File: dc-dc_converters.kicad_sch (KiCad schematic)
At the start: 61 parts, among them J3 JST_SH_1x4_SM04B-SRSS-TB-LF-SN, J4 Molex_Nano-Fit_1x2_105313-220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, U2 SIC477ED-T1-GE3, U3 AP62301WU-7, U4 AP62301WU-7

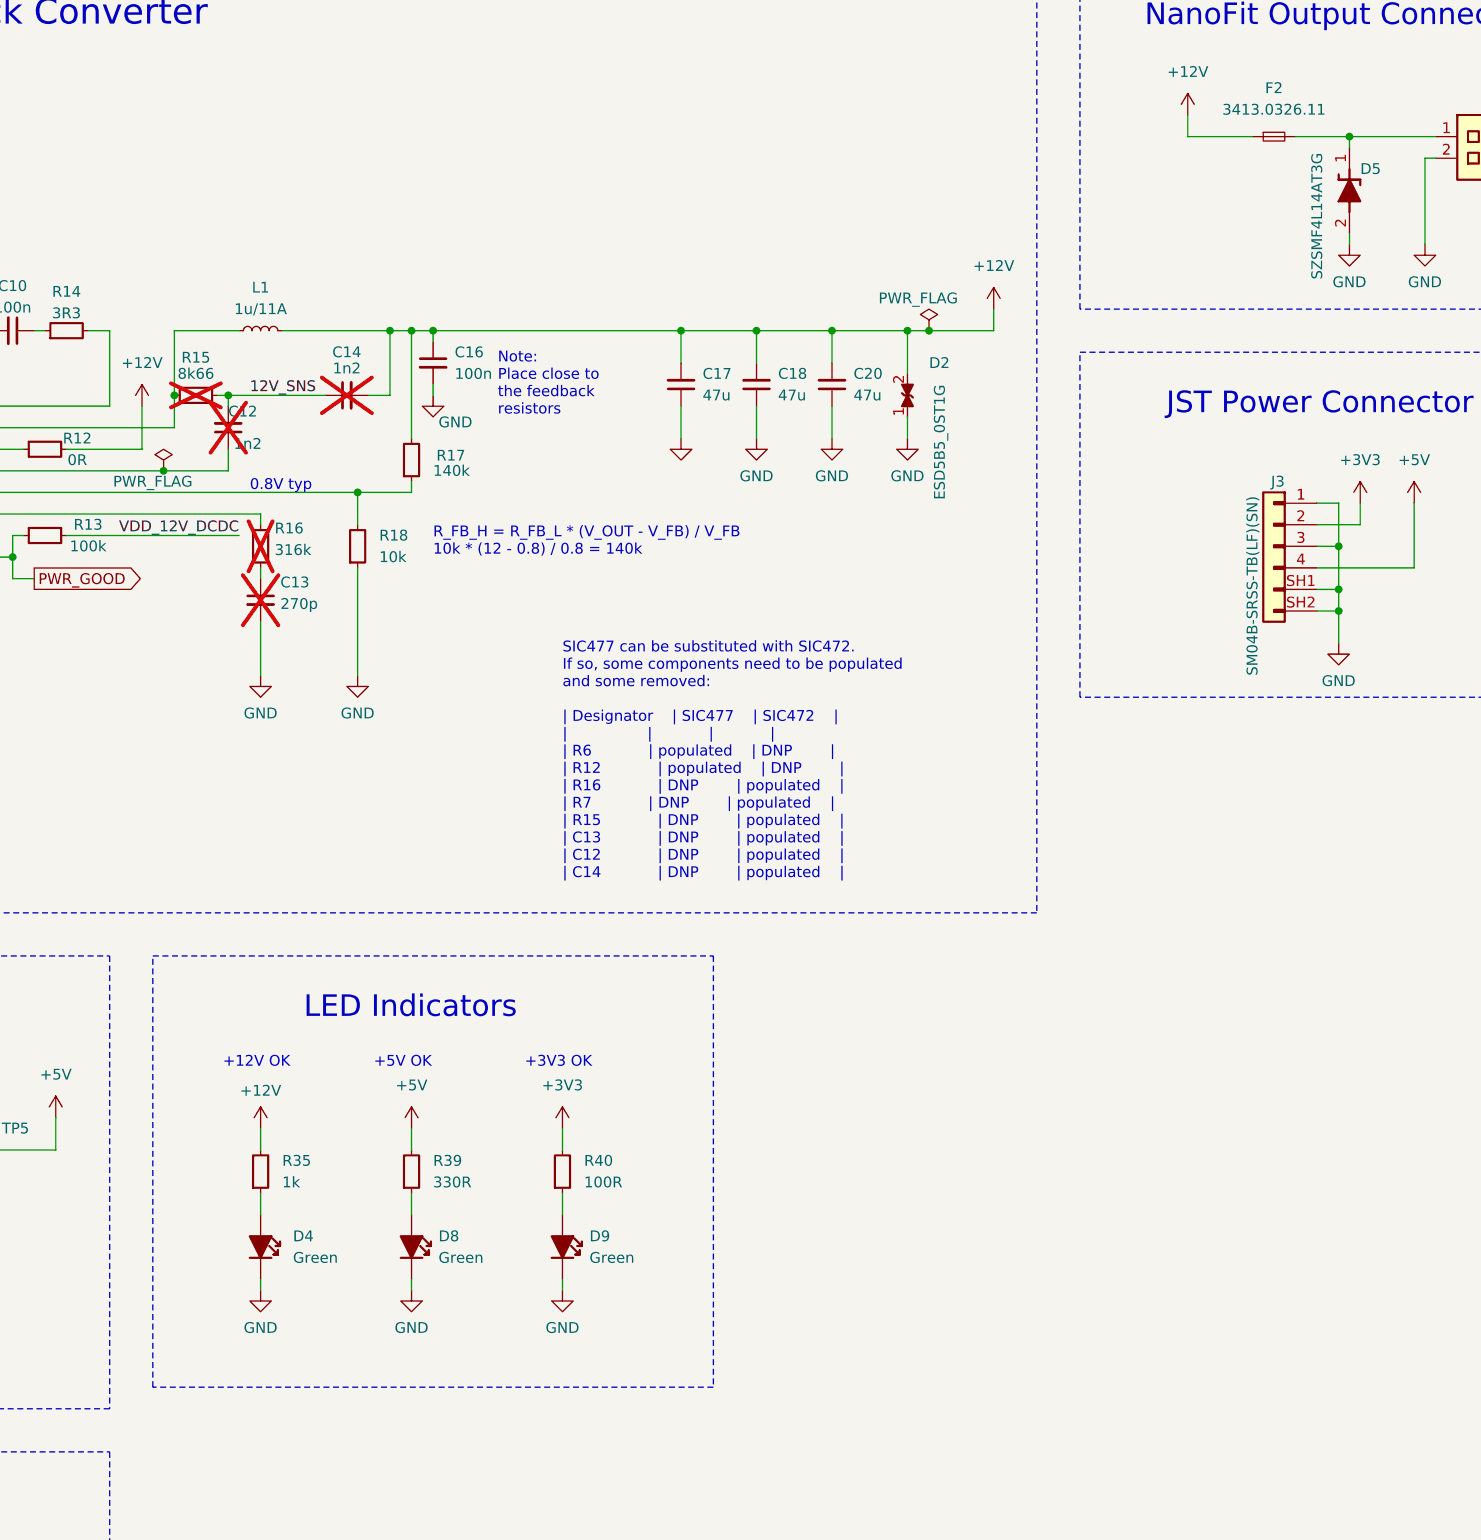
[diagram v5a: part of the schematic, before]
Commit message: [#57006] Change D5 to SZSMF4L12AT3G
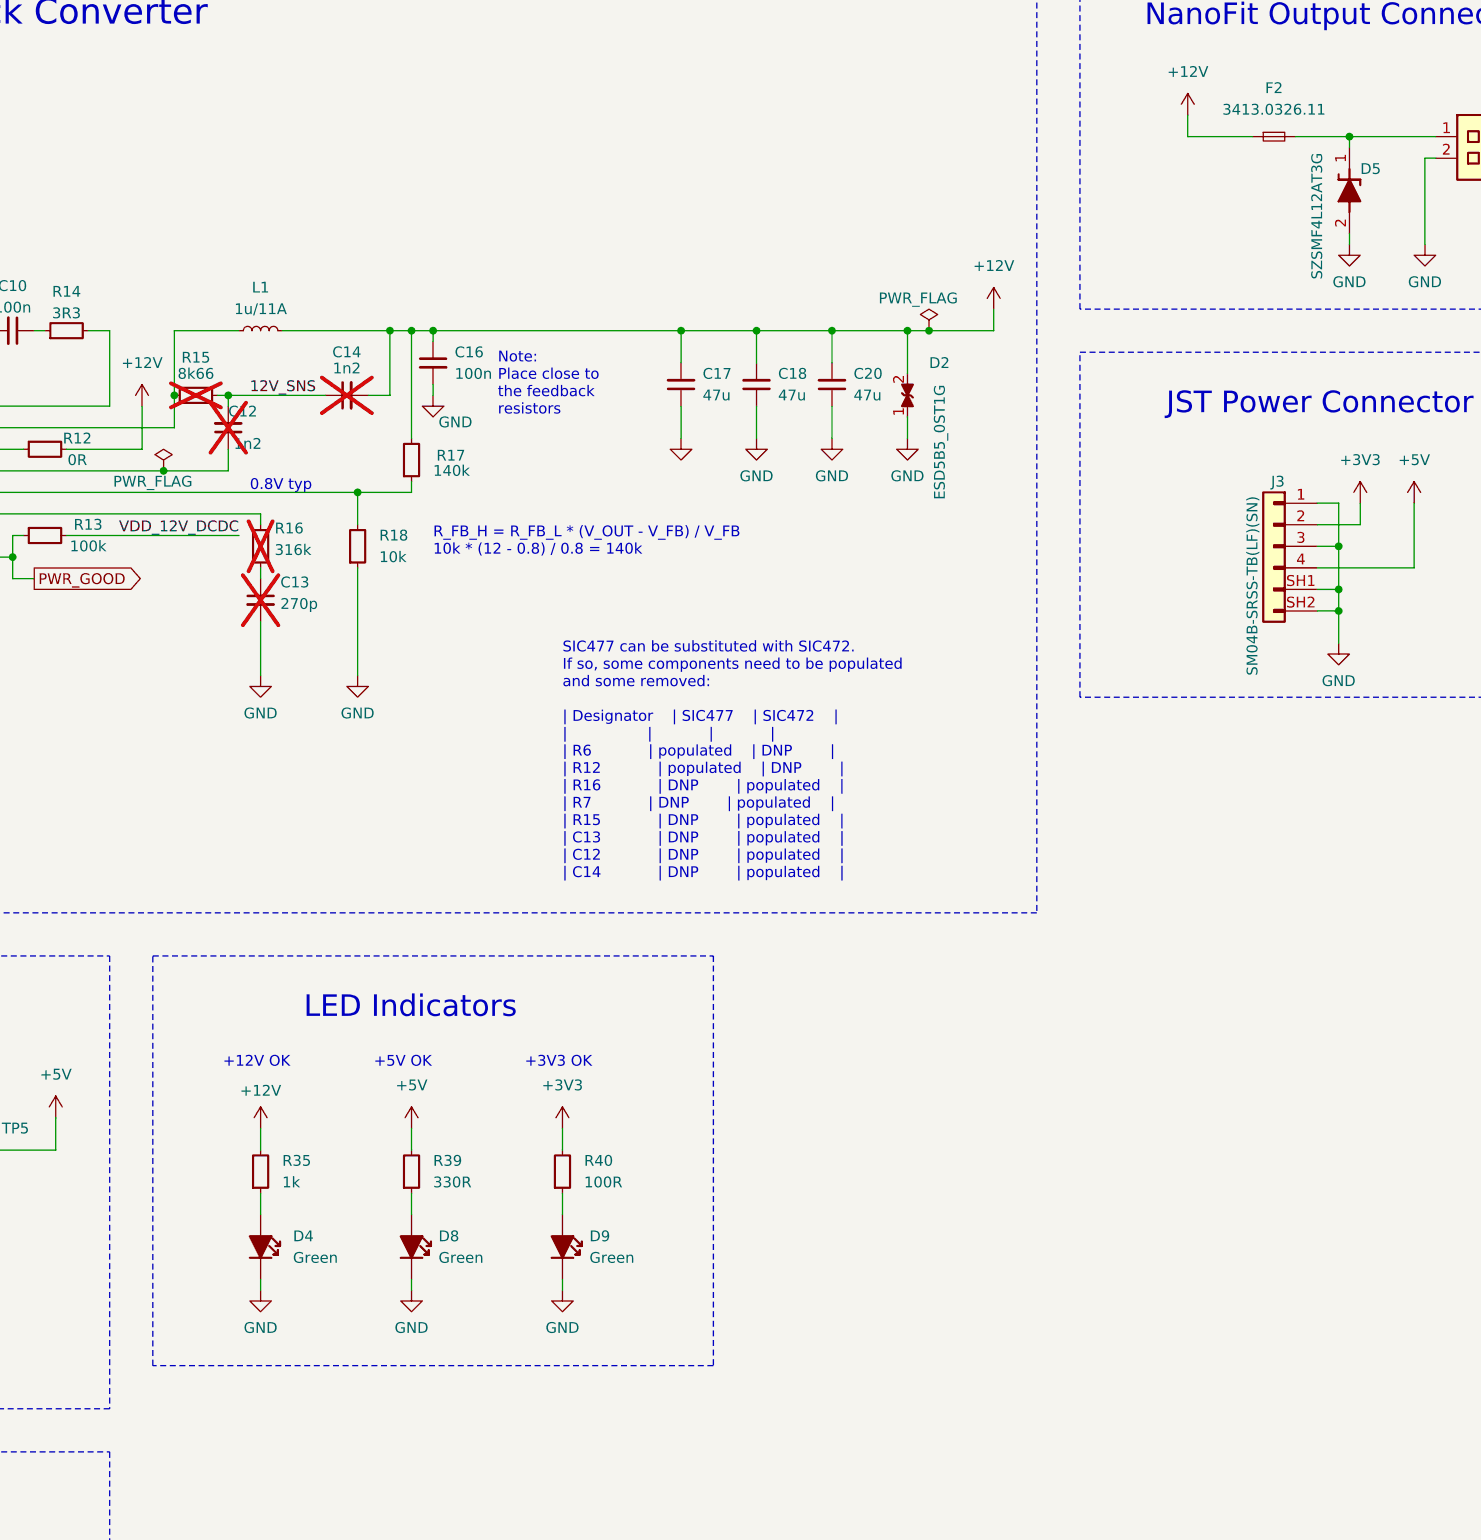
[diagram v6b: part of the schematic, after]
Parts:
- D5: value SZSMF4L14AT3G -> SZSMF4L12AT3G; MPN SZSMF4L14AT3G -> SZSMF4L12AT3G; Manufacturer Infineon -> (none)
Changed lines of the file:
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@@
     (fill (type none))
   )
-  (rectangle (start 165.1 147.32) (end 231.14 198.12)
+  (rectangle (start 165.1 147.32) (end 231.14 195.58)
     (stroke (width 0) (type dash))
     (fill (type none))
@@
       (effects (font (size 1.27 1.27) (thickness 0.15)) (justify right))
     )
-    (property "Value" "SZSMF4L14AT3G" (at 302.26 53.34 0)
+    (property "Value" "SZSMF4L12AT3G" (at 302.26 53.34 0)
       (effects (font (size 1.27 1.27) (thickness 0.15)) (justify right) hide)
     )
@@
       (effects (font (size 1.27 1.27) (thickness 0.15)) (justify left bottom) hide)
     )
-    (property "MPN" "SZSMF4L14AT3G" (at 302.26 52.705 0)
+    (property "MPN" "SZSMF4L12AT3G" (at 302.26 52.705 0)
       (effects (font (size 1.27 1.27)) (justify right))
     )
-    (property "Manufacturer" "Infineon" (at 323.85 35.56 0)
-      (effects (font (size 1.27 1.27) (thickness 0.15)) (justify left bottom) hide)
-    )
     (property "Author" "Antmicro" (at 326.39 35.56 0)

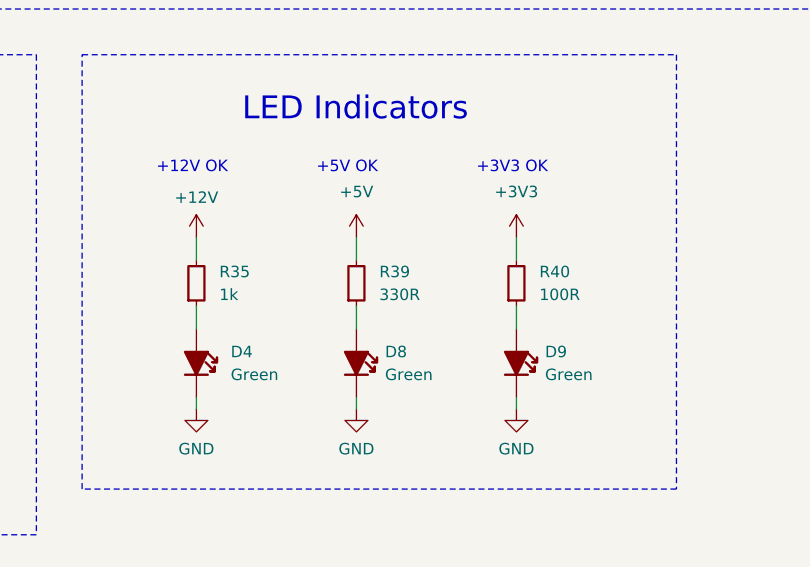
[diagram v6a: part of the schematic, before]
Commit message: [#57006] Change diodes' resistors
Decrease current
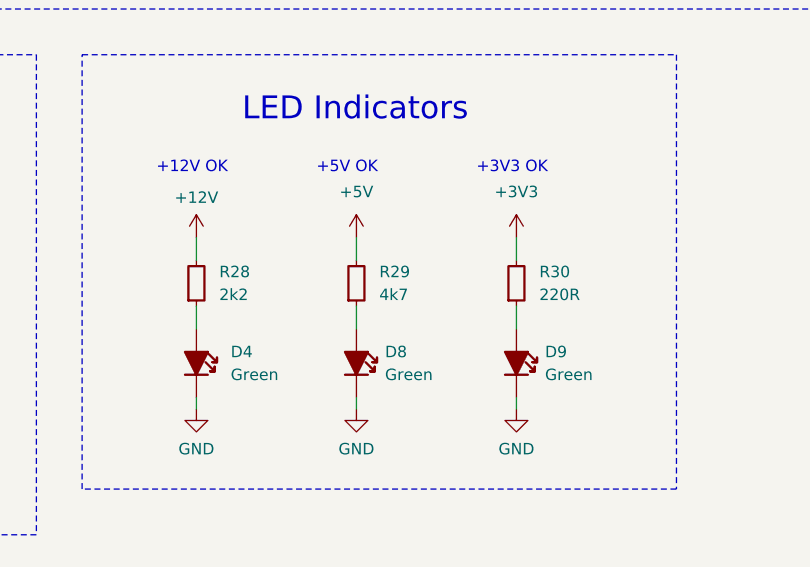
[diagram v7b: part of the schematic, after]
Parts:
- removed R35: R_2k2_0402, antmicro-footprints:R_0402_1005Metric, symbol antmicroResistors0402:R_1k_0402
- removed R39: R_330R_0402, antmicro-footprints:R_0402_1005Metric, symbol antmicroResistors0402:R_330R_0402
- removed R40: R_100R_0402, antmicro-footprints:R_0402_1005Metric, symbol antmicroResistors0402:R_100R_0402
- added R28: R_2k2_0402, antmicro-footprints:R_0402_1005Metric, symbol antmicroResistors0402:R_2k2_0402
- added R29: R_4k7_0402, antmicro-footprints:R_0402_1005Metric, symbol antmicroResistors0402:R_4k7_0402
- added R30: R_220R_0402, antmicro-footprints:R_0402_1005Metric, symbol antmicroResistors0402:R_220R_0402
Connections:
- net +12V: now also R28.2
- net +3V3: now also R30.2
- net +5V: now also R29.2
- net at D4.1: now also R28.1
- net at D8.1: now also R29.1
- net at D9.1: now also R30.1

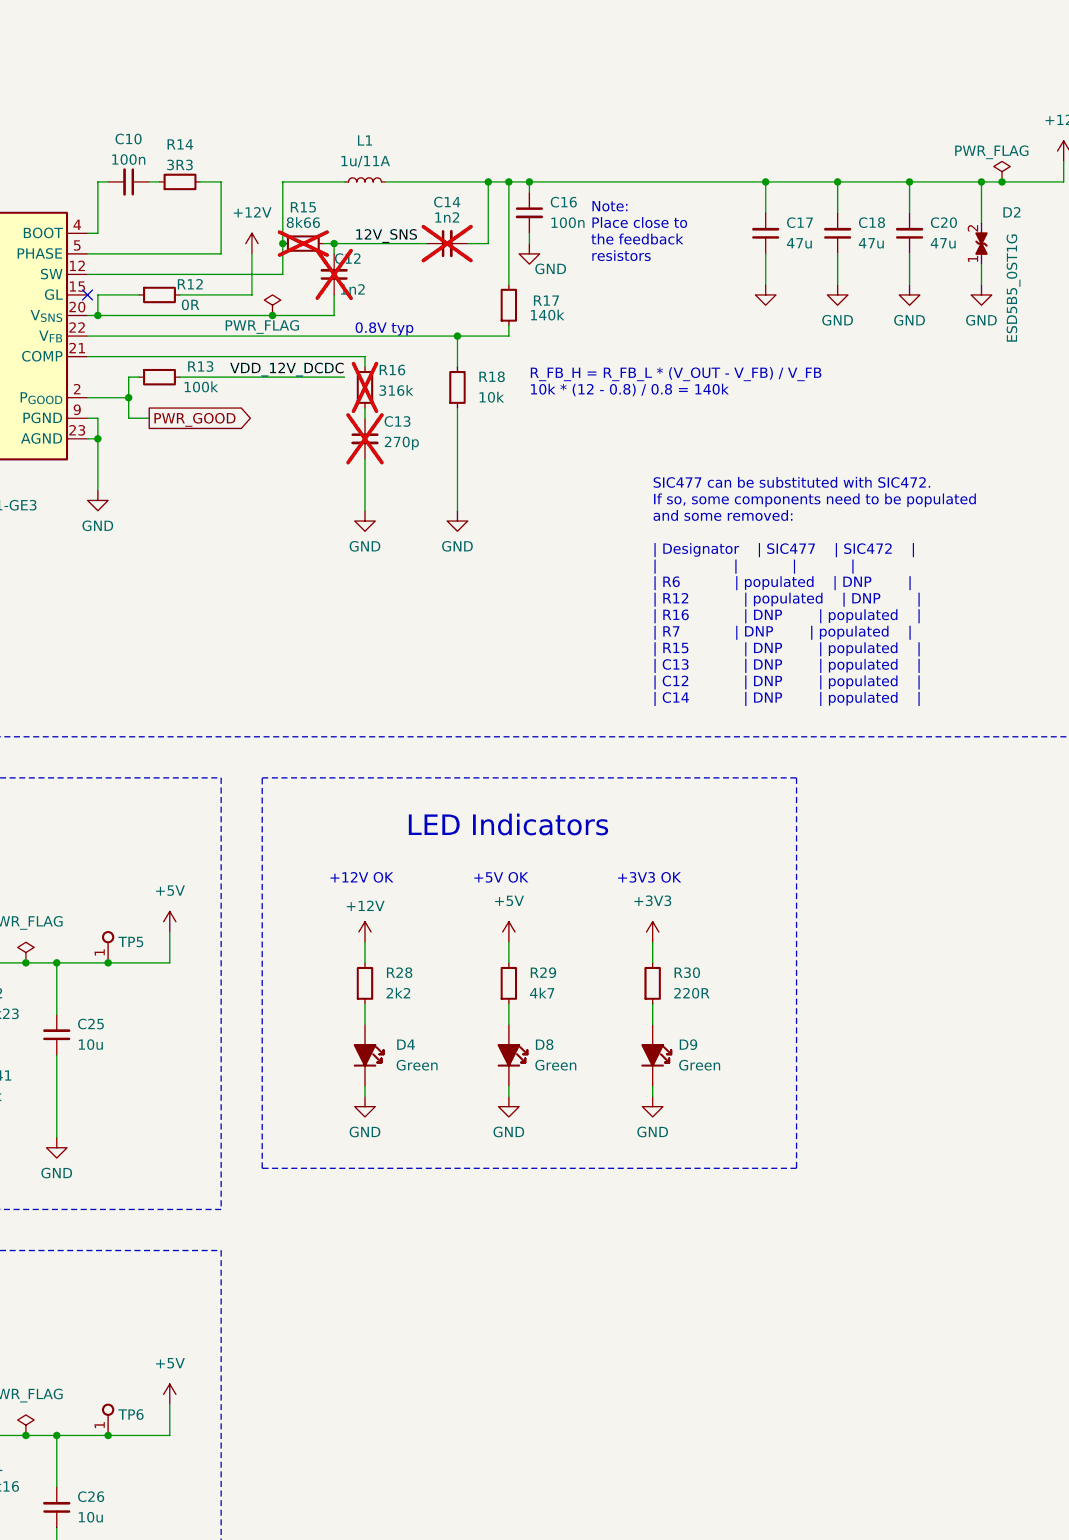
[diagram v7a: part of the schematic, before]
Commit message: [#57006] Fix wrong power label
Add +12V testpoint
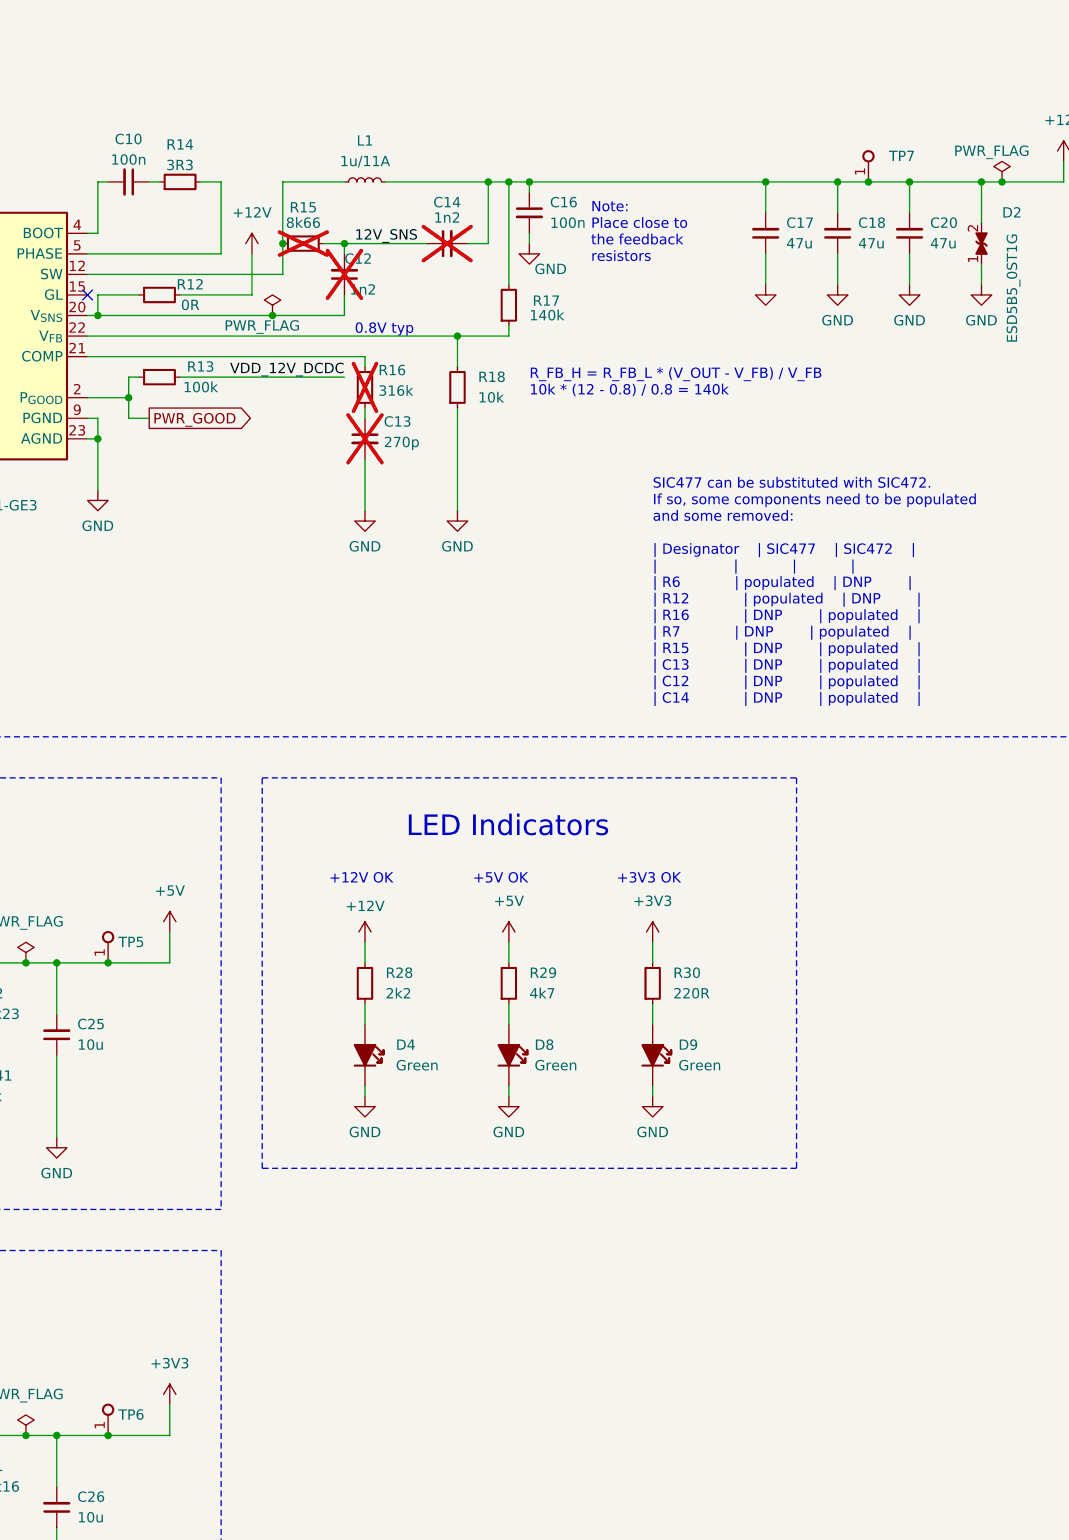
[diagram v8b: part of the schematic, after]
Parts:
- added TP7: TP_0.75mm_SMD, antmicro-footprints:TP_SMD_0.75mm, symbol antmicroTestPoints:TP_0.75mm_SMD
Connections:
- net +12V: now also TP7.1
- net +3V3: now also C26.2, L3.2, R1.2, TP6.1
- net +5V: no longer C26.2, L3.2, R1.2, TP6.1
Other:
- moved on the sheet: C12
